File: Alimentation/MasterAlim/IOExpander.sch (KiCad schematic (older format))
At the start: 12 parts, among them U8 PCF8574A

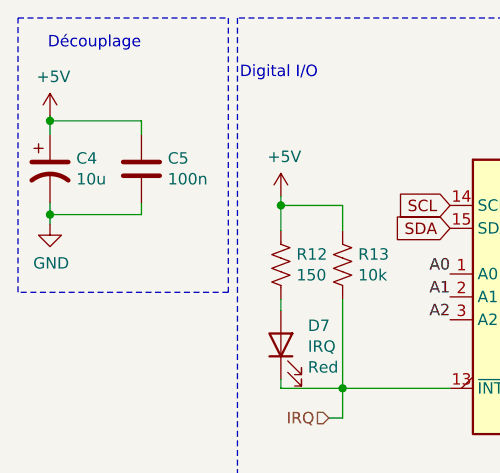
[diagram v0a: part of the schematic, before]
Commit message: Dimensionnement et récupération des part LCSC
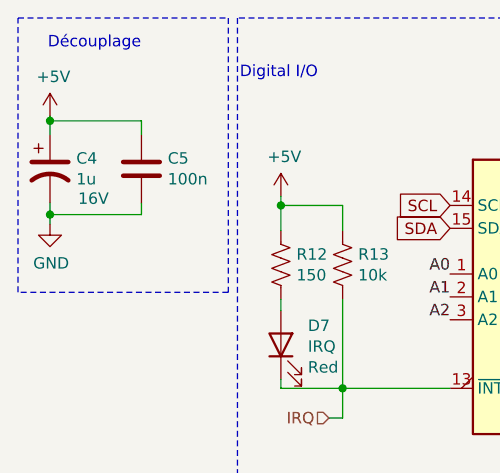
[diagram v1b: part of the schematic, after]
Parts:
- C4: value 10u -> 1u; footprint (none) -> Capacitor_SMD:CP_Elec_4x5.3; LCSC Part (none) -> C249445; Tension (none) -> 16V
- C5: footprint Capacitor_SMD:C_0805_2012Metric -> Capacitor_SMD:C_0805_2012Metric_Pad1.18x1.45mm_HandSolder; LCSC Part (none) -> C28233
- R12, R13, R14, R15, R16: footprint Resistor_SMD:R_0805_2012Metric -> Resistor_SMD:R_0805_2012Metric_Pad1.20x1.40mm_HandSolder
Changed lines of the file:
@@
 F 0 "R12" H 5308 4106 50  0000 L CNN
 F 1 "150" H 5308 4015 50  0000 L CNN
-F 2 "Resistor_SMD:R_0805_2012Metric" V 5280 4050 50  0001 C CNN
+F 2 "Resistor_SMD:R_0805_2012Metric_Pad1.20x1.40mm_HandSolder" V 5280 4050 50  0001 C CNN
 F 3 "~" H 5240 4060 50  0001 C CNN
 	1    5240 4060
@@
 F 0 "R13" H 5578 4106 50  0000 L CNN
 F 1 "10k" H 5578 4015 50  0000 L CNN
-F 2 "Resistor_SMD:R_0805_2012Metric" V 5550 4050 50  0001 C CNN
+F 2 "Resistor_SMD:R_0805_2012Metric_Pad1.20x1.40mm_HandSolder" V 5550 4050 50  0001 C CNN
 F 3 "~" H 5510 4060 50  0001 C CNN
 	1    5510 4060
@@
 F 0 "R14" H 7478 4356 50  0000 L CNN
 F 1 "10k" H 7478 4265 50  0000 L CNN
-F 2 "Resistor_SMD:R_0805_2012Metric" V 7450 4300 50  0001 C CNN
+F 2 "Resistor_SMD:R_0805_2012Metric_Pad1.20x1.40mm_HandSolder" V 7450 4300 50  0001 C CNN
 F 3 "~" H 7410 4310 50  0001 C CNN
 	1    7410 4310
@@
 F 0 "R15" H 7748 4356 50  0000 L CNN
 F 1 "10k" H 7748 4265 50  0000 L CNN
-F 2 "Resistor_SMD:R_0805_2012Metric" V 7720 4300 50  0001 C CNN
+F 2 "Resistor_SMD:R_0805_2012Metric_Pad1.20x1.40mm_HandSolder" V 7720 4300 50  0001 C CNN
 F 3 "~" H 7680 4310 50  0001 C CNN
 	1    7680 4310
@@
 F 0 "R16" H 8008 4356 50  0000 L CNN
 F 1 "10k" H 8008 4265 50  0000 L CNN
-F 2 "Resistor_SMD:R_0805_2012Metric" V 7980 4300 50  0001 C CNN
+F 2 "Resistor_SMD:R_0805_2012Metric_Pad1.20x1.40mm_HandSolder" V 7980 4300 50  0001 C CNN
 F 3 "~" H 7940 4310 50  0001 C CNN
 	1    7940 4310
@@
 F 0 "C5" H 4745 3686 50  0000 L CNN
 F 1 "100n" H 4745 3595 50  0000 L CNN
-F 2 "Capacitor_SMD:C_0805_2012Metric" H 4668 3490 50  0001 C CNN
+F 2 "Capacitor_SMD:C_0805_2012Metric_Pad1.18x1.45mm_HandSolder" H 4668 3490 50  0001 C CNN
 F 3 "~" H 4630 3640 50  0001 C CNN
+F 4 "C28233" H 4630 3640 50  0001 C CNN "LCSC Part"
 	1    4630 3640
 	1    0    0    -1
@@
 AR Path="/60C96C2B/60D8C4C7" Ref="C4"  Part="1"
 F 0 "C4" H 4345 3686 50  0000 L CNN
-F 1 "10u" H 4345 3595 50  0000 L CNN
-F 2 "" H 4230 3640 50  0001 C CNN
+F 1 "1u" H 4345 3595 50  0000 L CNN
+F 2 "Capacitor_SMD:CP_Elec_4x5.3" H 4230 3640 50  0001 C CNN
 F 3 "~" H 4230 3640 50  0001 C CNN
+F 4 "16V" H 4420 3510 50  0000 C CNN "Tension"
+F 5 "C249445" H 4230 3640 50  0001 C CNN "LCSC Part"
 	1    4230 3640
 	1    0    0    -1

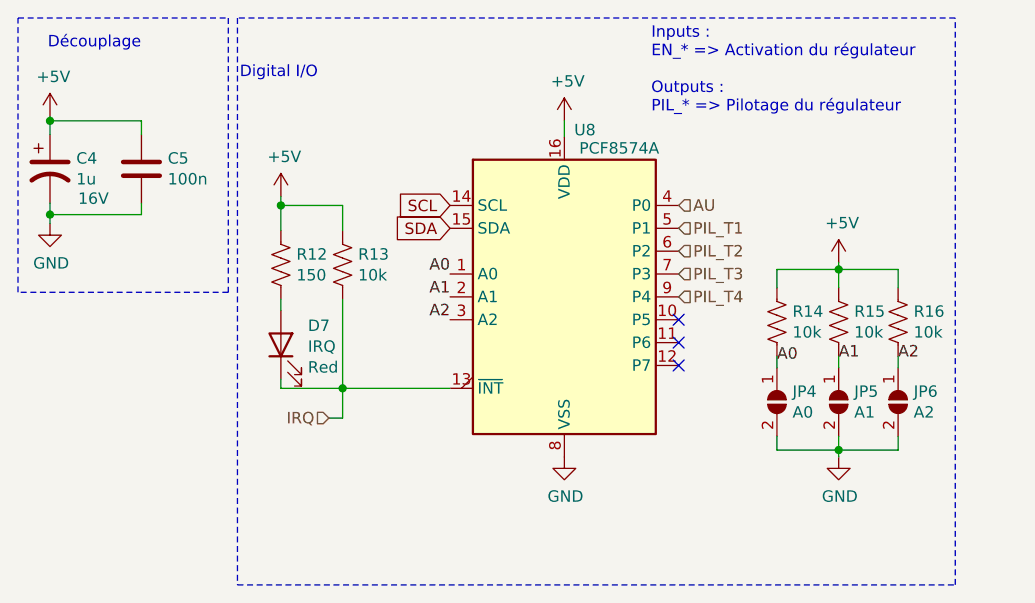
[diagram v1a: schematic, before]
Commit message: Finalisation routage carte alim maitre
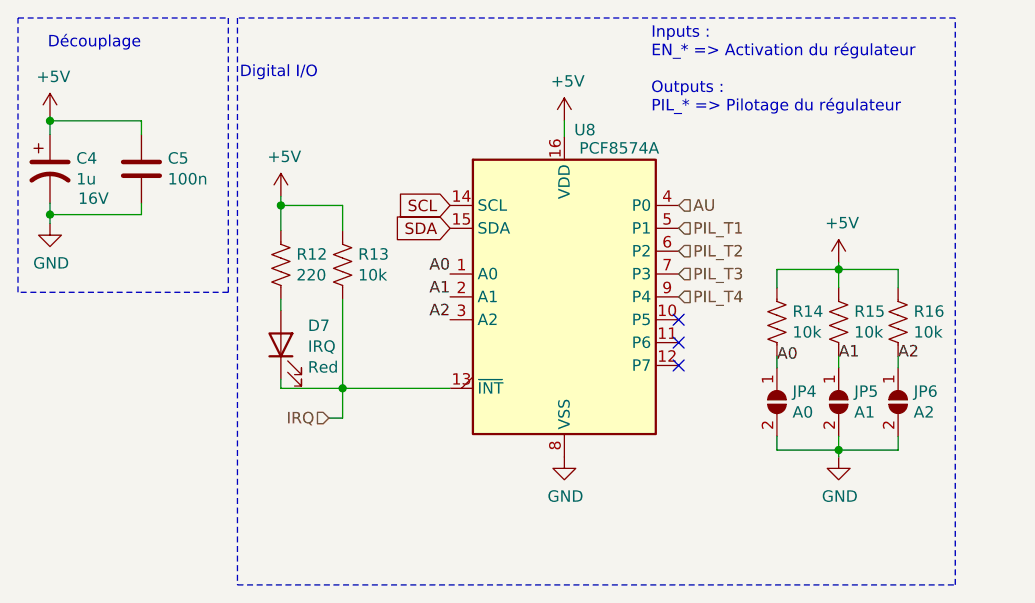
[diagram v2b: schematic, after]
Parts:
- JP4, JP5, JP6: footprint Jumper:SolderJumper-2_P1.3mm_Open_TrianglePad1.0x1.5mm -> Jumper:SolderJumper-2_P1.3mm_Open_RoundedPad1.0x1.5mm
- R12: value 150 -> 220; LCSC Part (none) -> C417010
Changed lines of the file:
@@
 AR Path="/60C96C2B/60CAA1DF" Ref="R12"  Part="1"
 F 0 "R12" H 5308 4106 50  0000 L CNN
-F 1 "150" H 5308 4015 50  0000 L CNN
+F 1 "220" H 5308 4015 50  0000 L CNN
 F 2 "Resistor_SMD:R_0805_2012Metric_Pad1.20x1.40mm_HandSolder" V 5280 4050 50  0001 C CNN
 F 3 "~" H 5240 4060 50  0001 C CNN
+F 4 "C417010" H 5240 4060 50  0001 C CNN "LCSC Part"
 	1    5240 4060
 	1    0    0    -1
@@
 F 0 "JP4" V 7364 4728 50  0000 L CNN
 F 1 "A0" V 7455 4728 50  0000 L CNN
-F 2 "Jumper:SolderJumper-2_P1.3mm_Open_TrianglePad1.0x1.5mm" H 7410 4660 50  0001 C CNN
+F 2 "Jumper:SolderJumper-2_P1.3mm_Open_RoundedPad1.0x1.5mm" H 7410 4660 50  0001 C CNN
 F 3 "~" H 7410 4660 50  0001 C CNN
 	1    7410 4660
@@
 F 0 "JP5" V 7634 4728 50  0000 L CNN
 F 1 "A1" V 7725 4728 50  0000 L CNN
-F 2 "Jumper:SolderJumper-2_P1.3mm_Open_TrianglePad1.0x1.5mm" H 7680 4660 50  0001 C CNN
+F 2 "Jumper:SolderJumper-2_P1.3mm_Open_RoundedPad1.0x1.5mm" H 7680 4660 50  0001 C CNN
 F 3 "~" H 7680 4660 50  0001 C CNN
 	1    7680 4660
@@
 F 0 "JP6" V 7894 4728 50  0000 L CNN
 F 1 "A2" V 7985 4728 50  0000 L CNN
-F 2 "Jumper:SolderJumper-2_P1.3mm_Open_TrianglePad1.0x1.5mm" H 7940 4660 50  0001 C CNN
+F 2 "Jumper:SolderJumper-2_P1.3mm_Open_RoundedPad1.0x1.5mm" H 7940 4660 50  0001 C CNN
 F 3 "~" H 7940 4660 50  0001 C CNN
 	1    7940 4660

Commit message: Module alim ISO, clean master alim
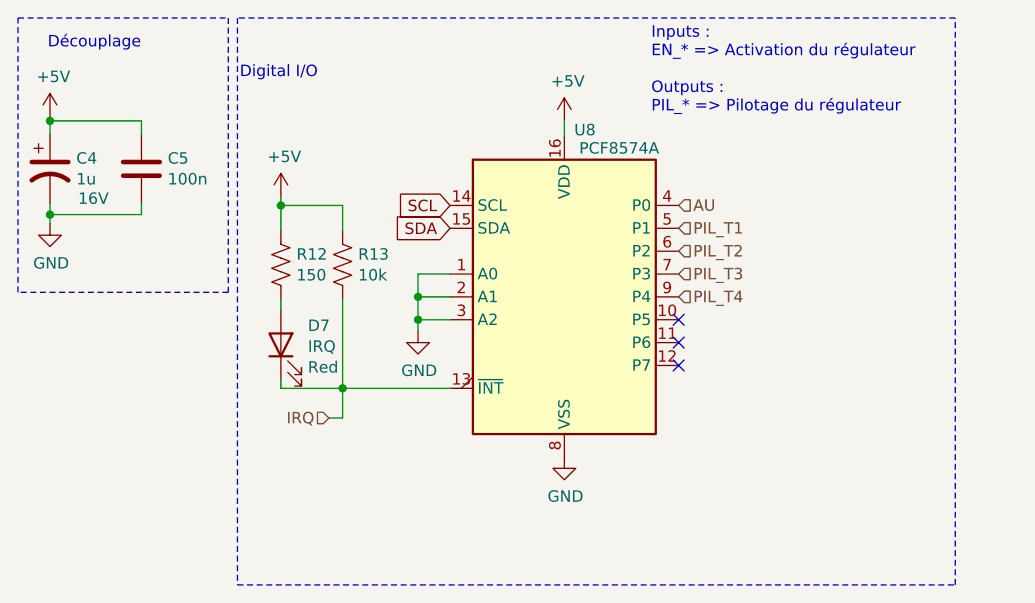
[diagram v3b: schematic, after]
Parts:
- removed JP4: A0, Jumper:SolderJumper-2_P1.3mm_Open_RoundedPad1.0x1.5mm, symbol Jumper:SolderJumper_2_Open
- removed JP5: A1, Jumper:SolderJumper-2_P1.3mm_Open_RoundedPad1.0x1.5mm, symbol Jumper:SolderJumper_2_Open
- removed JP6: A2, Jumper:SolderJumper-2_P1.3mm_Open_RoundedPad1.0x1.5mm, symbol Jumper:SolderJumper_2_Open
- removed R14, R15, R16: 10k, Resistor_SMD:R_0805_2012Metric_Pad1.20x1.40mm_HandSolder, symbol Device:R_US
- C5: footprint Capacitor_SMD:C_0805_2012Metric_Pad1.18x1.45mm_HandSolder -> Capacitor_SMD:C_0603_1608Metric_Pad1.08x0.95mm_HandSolder; LCSC Part C28233 -> C80516; Tension (none) -> 16V
- D7: LCSC Part (none) -> C72037
- R12: value 220 -> 150; LCSC Part C417010 -> C17471
- R13: LCSC Part (none) -> C17414
- U8: LCSC Part (none) -> C86832
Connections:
- net A0 is gone; now on net GND: U8.1 (A0)
- net A1 is gone; now on net GND: U8.2 (A1)
- net A2 is gone; now on net GND: U8.3 (A2)
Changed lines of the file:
@@
 AR Path="/60C96C2B/60CAA1DF" Ref="R12"  Part="1"
 F 0 "R12" H 5308 4106 50  0000 L CNN
-F 1 "220" H 5308 4015 50  0000 L CNN
+F 1 "150" H 5308 4015 50  0000 L CNN
 F 2 "Resistor_SMD:R_0805_2012Metric_Pad1.20x1.40mm_HandSolder" V 5280 4050 50  0001 C CNN
 F 3 "~" H 5240 4060 50  0001 C CNN
-F 4 "C417010" H 5240 4060 50  0001 C CNN "LCSC Part"
+F 4 "C17471" H 5240 4060 50  0001 C CNN "LCSC Part"
 	1    5240 4060
 	1    0    0    -1
@@
 F 2 "Resistor_SMD:R_0805_2012Metric_Pad1.20x1.40mm_HandSolder" V 5550 4050 50  0001 C CNN
 F 3 "~" H 5510 4060 50  0001 C CNN
+F 4 "C17414" H 5510 4060 50  0001 C CNN "LCSC Part"
 	1    5510 4060
 	1    0    0    -1
@@
 	5240 3800 5240 3760
 $Comp
-L power:GND #PWR?
-U 1 1 60CAA1F6
-P 7680 4900
-AR Path="/60CAA1F6" Ref="#PWR?"  Part="1"
-AR Path="/60C96C2B/60CAA1F6" Ref="#PWR0125"  Part="1"
-F 0 "#PWR0125" H 7680 4650 50  0001 C CNN
-F 1 "GND" H 7685 4727 50  0000 C CNN
-F 2 "" H 7680 4900 50  0001 C CNN
-F 3 "" H 7680 4900 50  0001 C CNN
-	1    7680 4900
-	1    0    0    -1
-$EndComp
-$Comp
 L Device:LED D?
 U 1 1 60CAA1FD
@@
 F 3 "~" H 5240 4410 50  0001 C CNN
 F 4 "Red" V 5142 4292 50  0000 R CNN "Color"
+F 5 "C72037" H 5240 4410 50  0001 C CNN "LCSC Part"
 	1    5240 4410
 	0    -1   -1   0
@@
 Wire Wire Line
 	5240 4600 5240 4560
-$Comp
-L Jumper:SolderJumper_2_Open JP?
-U 1 1 60CAA209
-P 7410 4660
-AR Path="/60CAA209" Ref="JP?"  Part="1"
-AR Path="/60C96C2B/60CAA209" Ref="JP4"  Part="1"
-F 0 "JP4" V 7364 4728 50  0000 L CNN
-F 1 "A0" V 7455 4728 50  0000 L CNN
-F 2 "Jumper:SolderJumper-2_P1.3mm_Open_RoundedPad1.0x1.5mm" H 7410 4660 50  0001 C CNN
-F 3 "~" H 7410 4660 50  0001 C CNN
-	1    7410 4660
-	0    1    1    0
-$EndComp
-$Comp
-L Jumper:SolderJumper_2_Open JP?
-U 1 1 60CAA20F
-P 7680 4660
-AR Path="/60CAA20F" Ref="JP?"  Part="1"
-AR Path="/60C96C2B/60CAA20F" Ref="JP5"  Part="1"
-F 0 "JP5" V 7634 4728 50  0000 L CNN
-F 1 "A1" V 7725 4728 50  0000 L CNN
-F 2 "Jumper:SolderJumper-2_P1.3mm_Open_RoundedPad1.0x1.5mm" H 7680 4660 50  0001 C CNN
-F 3 "~" H 7680 4660 50  0001 C CNN
-	1    7680 4660
-	0    1    1    0
-$EndComp
-$Comp
-L Jumper:SolderJumper_2_Open JP?
-U 1 1 60CAA215
-P 7940 4660
-AR Path="/60CAA215" Ref="JP?"  Part="1"
-AR Path="/60C96C2B/60CAA215" Ref="JP6"  Part="1"
-F 0 "JP6" V 7894 4728 50  0000 L CNN
-F 1 "A2" V 7985 4728 50  0000 L CNN
-F 2 "Jumper:SolderJumper-2_P1.3mm_Open_RoundedPad1.0x1.5mm" H 7940 4660 50  0001 C CNN
-F 3 "~" H 7940 4660 50  0001 C CNN
-	1    7940 4660
-	0    1    1    0
-$EndComp
-Wire Wire Line
-	7940 4810 7940 4870
-Wire Wire Line
-	7940 4870 7680 4870
-Wire Wire Line
-	7410 4870 7410 4810
-Wire Wire Line
-	7680 4810 7680 4870
-Connection ~ 7680 4870
-Wire Wire Line
-	7680 4870 7410 4870
-$Comp
-L Device:R_US R?
-U 1 1 60CAA223
-P 7410 4310
-AR Path="/60CAA223" Ref="R?"  Part="1"
-AR Path="/60C96C2B/60CAA223" Ref="R14"  Part="1"
-F 0 "R14" H 7478 4356 50  0000 L CNN
-F 1 "10k" H 7478 4265 50  0000 L CNN
-F 2 "Resistor_SMD:R_0805_2012Metric_Pad1.20x1.40mm_HandSolder" V 7450 4300 50  0001 C CNN
-F 3 "~" H 7410 4310 50  0001 C CNN
-	1    7410 4310
-	1    0    0    -1
-$EndComp
-$Comp
-L Device:R_US R?
-U 1 1 60CAA229
-P 7680 4310
-AR Path="/60CAA229" Ref="R?"  Part="1"
-AR Path="/60C96C2B/60CAA229" Ref="R15"  Part="1"
-F 0 "R15" H 7748 4356 50  0000 L CNN
-F 1 "10k" H 7748 4265 50  0000 L CNN
-F 2 "Resistor_SMD:R_0805_2012Metric_Pad1.20x1.40mm_HandSolder" V 7720 4300 50  0001 C CNN
-F 3 "~" H 7680 4310 50  0001 C CNN
-	1    7680 4310
-	1    0    0    -1
-$EndComp
-$Comp
-L Device:R_US R?
-U 1 1 60CAA22F
-P 7940 4310
-AR Path="/60CAA22F" Ref="R?"  Part="1"
-AR Path="/60C96C2B/60CAA22F" Ref="R16"  Part="1"
-F 0 "R16" H 8008 4356 50  0000 L CNN
-F 1 "10k" H 8008 4265 50  0000 L CNN
-F 2 "Resistor_SMD:R_0805_2012Metric_Pad1.20x1.40mm_HandSolder" V 7980 4300 50  0001 C CNN
-F 3 "~" H 7940 4310 50  0001 C CNN
-	1    7940 4310
-	1    0    0    -1
-$EndComp
-Wire Wire Line
-	7410 4160 7410 4080
-Wire Wire Line
-	7940 4160 7940 4080
-Wire Wire Line
-	7940 4080 7680 4080
-Wire Wire Line
-	7680 4160 7680 4080
-Connection ~ 7680 4080
-Wire Wire Line
-	7680 4080 7410 4080
-Wire Wire Line
-	7410 4510 7410 4460
-Wire Wire Line
-	7680 4510 7680 4460
-Wire Wire Line
-	7940 4510 7940 4460
-Text Label 7410 4490 0    50   ~ 0
-A0
-Text Label 7680 4480 0    50   ~ 0
-A1
-Text Label 7940 4480 0    50   ~ 0
-A2
-Text Label 5980 4100 2    50   ~ 0
-A0
-Text Label 5980 4200 2    50   ~ 0
-A1
-Text Label 5980 4300 2    50   ~ 0
-A2
 Text GLabel 5980 3800 0    50   Input ~ 0
 SCL
@@
 Text HLabel 6980 3800 2    50   Input ~ 0
 AU
-$Comp
-L power:+5V #PWR?
-U 1 1 60CC1A30
-P 7680 4050
-AR Path="/60CC1A30" Ref="#PWR?"  Part="1"
-AR Path="/60C96C2B/60CC1A30" Ref="#PWR0126"  Part="1"
-F 0 "#PWR0126" H 7680 3900 50  0001 C CNN
-F 1 "+5V" H 7695 4223 50  0000 C CNN
-F 2 "" H 7680 4050 50  0001 C CNN
-F 3 "" H 7680 4050 50  0001 C CNN
-	1    7680 4050
-	1    0    0    -1
-$EndComp
-Wire Wire Line
-	7680 4050 7680 4080
-Wire Wire Line
-	7680 4900 7680 4870
 Connection ~ 5510 4600
 Text HLabel 6980 3900 2    50   Input ~ 0
@@
 F 0 "C5" H 4745 3686 50  0000 L CNN
 F 1 "100n" H 4745 3595 50  0000 L CNN
-F 2 "Capacitor_SMD:C_0805_2012Metric_Pad1.18x1.45mm_HandSolder" H 4668 3490 50  0001 C CNN
+F 2 "Capacitor_SMD:C_0603_1608Metric_Pad1.08x0.95mm_HandSolder" H 4668 3490 50  0001 C CNN
 F 3 "~" H 4630 3640 50  0001 C CNN
-F 4 "C28233" H 4630 3640 50  0001 C CNN "LCSC Part"
+F 4 "C80516" H 4630 3640 50  0001 C CNN "LCSC Part"
+F 5 "16V" H 4630 3640 50  0001 C CNN "Tension"
 	1    4630 3640
 	1    0    0    -1
@@
 F 2 "Package_SO:SOIC-16W_7.5x10.3mm_P1.27mm" H 6480 4200 50  0001 C CNN
 F 3 "http://www.nxp.com/documents/data_sheet/PCF8574_PCF8574A.pdf" H 6480 4200 50  0001 C CNN
+F 4 "C86832" H 6480 4200 50  0001 C CNN "LCSC Part"
 	1    6480 4200
 	1    0    0    -1
@@
 NoConn ~ 6980 4400
 NoConn ~ 6980 4500
+$Comp
+L power:GND #PWR?
+U 1 1 5FEB6CA5
+P 5840 4350
+AR Path="/5FEB6CA5" Ref="#PWR?"  Part="1"
+AR Path="/60C96C2B/5FEB6CA5" Ref="#PWR032"  Part="1"
+F 0 "#PWR032" H 5840 4100 50  0001 C CNN
+F 1 "GND" H 5845 4177 50  0000 C CNN
+F 2 "" H 5840 4350 50  0001 C CNN
+F 3 "" H 5840 4350 50  0001 C CNN
+	1    5840 4350
+	1    0    0    -1
+$EndComp
+Wire Wire Line
+	5980 4100 5840 4100
+Wire Wire Line
+	5840 4100 5840 4200
+Wire Wire Line
+	5980 4300 5840 4300
+Connection ~ 5840 4300
+Wire Wire Line
+	5840 4300 5840 4350
+Wire Wire Line
+	5980 4200 5840 4200
+Connection ~ 5840 4200
+Wire Wire Line
+	5840 4200 5840 4300
 $EndSCHEMATC

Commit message: Finalisation alimentations
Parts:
- removed C4: 1u, Capacitor_SMD:CP_Elec_4x5.3, symbol Device:CP1
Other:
- moved on the sheet: C5
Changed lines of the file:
@@
 L Device:C C?
 U 1 1 60D8C4C1
-P 4630 3640
+P 4530 3650
 AR Path="/60D8C4C1" Ref="C?"  Part="1"
 AR Path="/60C96C2B/60D8C4C1" Ref="C5"  Part="1"
-F 0 "C5" H 4745 3686 50  0000 L CNN
-F 1 "100n" H 4745 3595 50  0000 L CNN
-F 2 "Capacitor_SMD:C_0603_1608Metric_Pad1.08x0.95mm_HandSolder" H 4668 3490 50  0001 C CNN
-F 3 "~" H 4630 3640 50  0001 C CNN
-F 4 "C80516" H 4630 3640 50  0001 C CNN "LCSC Part"
-F 5 "16V" H 4630 3640 50  0001 C CNN "Tension"
-	1    4630 3640
-	1    0    0    -1
-$EndComp
-$Comp
-L Device:CP1 C?
-U 1 1 60D8C4C7
-P 4230 3640
-AR Path="/60D8C4C7" Ref="C?"  Part="1"
-AR Path="/60C96C2B/60D8C4C7" Ref="C4"  Part="1"
-F 0 "C4" H 4345 3686 50  0000 L CNN
-F 1 "1u" H 4345 3595 50  0000 L CNN
-F 2 "Capacitor_SMD:CP_Elec_4x5.3" H 4230 3640 50  0001 C CNN
-F 3 "~" H 4230 3640 50  0001 C CNN
-F 4 "16V" H 4420 3510 50  0000 C CNN "Tension"
-F 5 "C249445" H 4230 3640 50  0001 C CNN "LCSC Part"
-	1    4230 3640
+F 0 "C5" H 4645 3696 50  0000 L CNN
+F 1 "100n" H 4645 3605 50  0000 L CNN
+F 2 "Capacitor_SMD:C_0603_1608Metric_Pad1.08x0.95mm_HandSolder" H 4568 3500 50  0001 C CNN
+F 3 "~" H 4530 3650 50  0001 C CNN
+F 4 "C80516" H 4530 3650 50  0001 C CNN "LCSC Part"
+F 5 "16V" H 4530 3650 50  0001 C CNN "Tension"
+	1    4530 3650
 	1    0    0    -1
 $EndComp
@@
 L power:+5V #PWR?
 U 1 1 60D8C4CD
-P 4230 3410
+P 4530 3500
 AR Path="/60D8C4CD" Ref="#PWR?"  Part="1"
 AR Path="/60C96C2B/60D8C4CD" Ref="#PWR0127"  Part="1"
-F 0 "#PWR0127" H 4230 3260 50  0001 C CNN
-F 1 "+5V" H 4245 3583 50  0000 C CNN
-F 2 "" H 4230 3410 50  0001 C CNN
-F 3 "" H 4230 3410 50  0001 C CNN
-	1    4230 3410
+F 0 "#PWR0127" H 4530 3350 50  0001 C CNN
+F 1 "+5V" H 4545 3673 50  0000 C CNN
+F 2 "" H 4530 3500 50  0001 C CNN
+F 3 "" H 4530 3500 50  0001 C CNN
+	1    4530 3500
 	1    0    0    -1
 $EndComp
@@
 L power:GND #PWR?
 U 1 1 60D8C4D3
-P 4230 3880
+P 4530 3800
 AR Path="/60D8C4D3" Ref="#PWR?"  Part="1"
 AR Path="/60C96C2B/60D8C4D3" Ref="#PWR0128"  Part="1"
-F 0 "#PWR0128" H 4230 3630 50  0001 C CNN
-F 1 "GND" H 4235 3707 50  0000 C CNN
-F 2 "" H 4230 3880 50  0001 C CNN
-F 3 "" H 4230 3880 50  0001 C CNN
-	1    4230 3880
+F 0 "#PWR0128" H 4530 3550 50  0001 C CNN
+F 1 "GND" H 4535 3627 50  0000 C CNN
+F 2 "" H 4530 3800 50  0001 C CNN
+F 3 "" H 4530 3800 50  0001 C CNN
+	1    4530 3800
 	1    0    0    -1
 $EndComp
-Wire Wire Line
-	4230 3490 4230 3430
-Wire Wire Line
-	4230 3880 4230 3840
-Connection ~ 4230 3840
-Wire Wire Line
-	4230 3840 4230 3790
-Wire Wire Line
-	4630 3790 4630 3840
-Wire Wire Line
-	4630 3840 4230 3840
-Connection ~ 4230 3430
-Wire Wire Line
-	4230 3430 4230 3410
-Wire Wire Line
-	4630 3490 4630 3430
-Wire Wire Line
-	4630 3430 4230 3430
-Text Notes 4220 3120 0    50   ~ 0
+Text Notes 4320 3130 0    50   ~ 0
 Découplage
 Wire Notes Line

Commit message: Finalisation pour commande pack Alimentation 14/02/2021
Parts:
- C5: LCSC Part C80516 -> C14663; Tension 16V -> 50V
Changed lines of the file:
@@
 F 2 "Capacitor_SMD:C_0603_1608Metric_Pad1.08x0.95mm_HandSolder" H 4568 3500 50  0001 C CNN
 F 3 "~" H 4530 3650 50  0001 C CNN
-F 4 "C80516" H 4530 3650 50  0001 C CNN "LCSC Part"
-F 5 "16V" H 4530 3650 50  0001 C CNN "Tension"
+F 4 " C14663" H 4530 3650 50  0001 C CNN "LCSC Part"
+F 5 "50V" H 4530 3650 50  0001 C CNN "Tension"
 	1    4530 3650
 	1    0    0    -1
